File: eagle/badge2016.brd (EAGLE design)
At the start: 135 x 100.5 mm, 123 parts, among them IC1 25AA080SN, IC2 FT231XQ, J1 USB-MICRO, Q2 BC857ALT1SMD, Q2_24MHZ NX5032G, X1 PASSER-07, X10 PAD-1.27X1.27, X12 PAD-1.27X1.27, X13 PAD-1.27X1.27, X14 PAD-1.27X1.27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

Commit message: Final Badge!
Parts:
- added R13, R14: 100k, we-rcl:C0402
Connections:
- new net N$33: IC1.7, R14.2
- new net N$38: IC1.3, R13.2
- net 3V3: now also R13.1, R14.1
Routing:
- net N$38: track 0.00 -> 5.61 mm
- net EEPROM_!CS: track 27.8 -> 22.5 mm
- net N$33: track 0.00 -> 3.96 mm
- net 3V3: track 325.7 -> 329.2 mm
- net SPI_MOSI: track 82.3 -> 85.4 mm
- net SPI_MISO: track 63.0 -> 61.9 mm
- net GND: vias 354 -> 353
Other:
- board text added: "Silkscreen: T_PRINT 100 and B_PRINT 101"

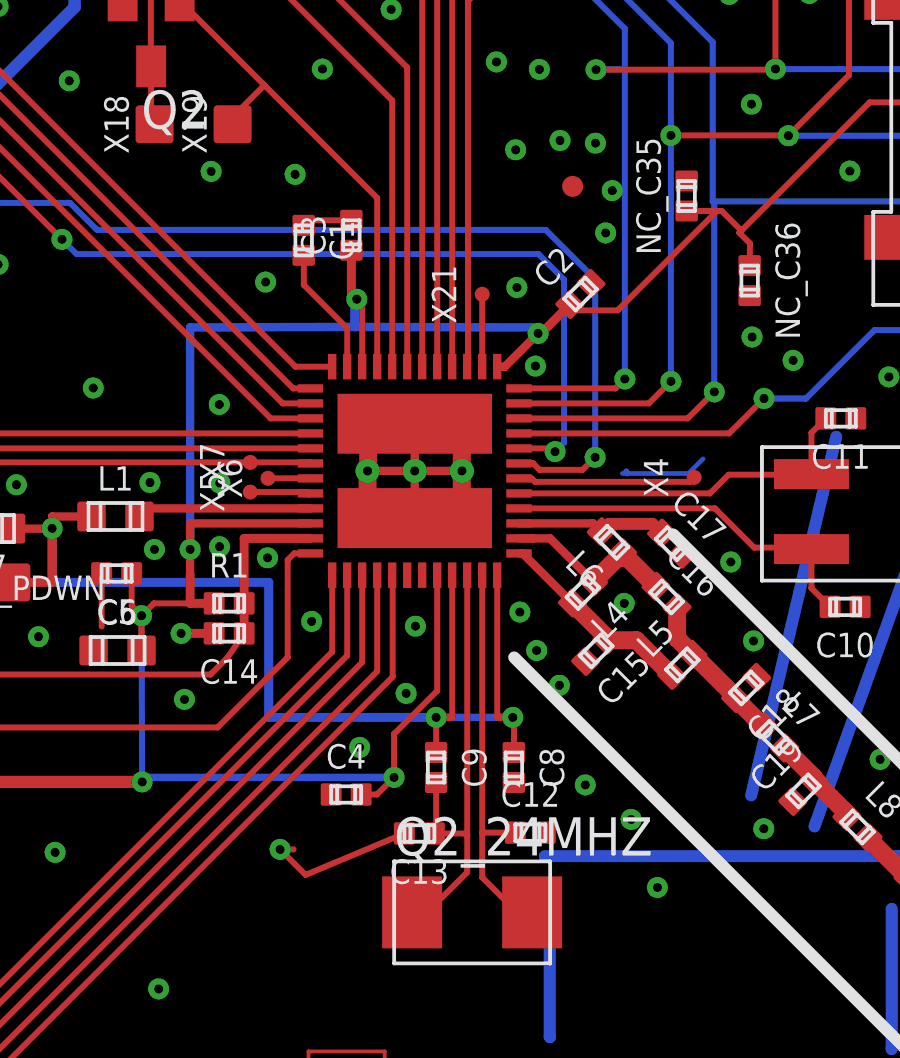
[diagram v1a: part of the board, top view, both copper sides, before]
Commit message: final badge with fixes from watterott
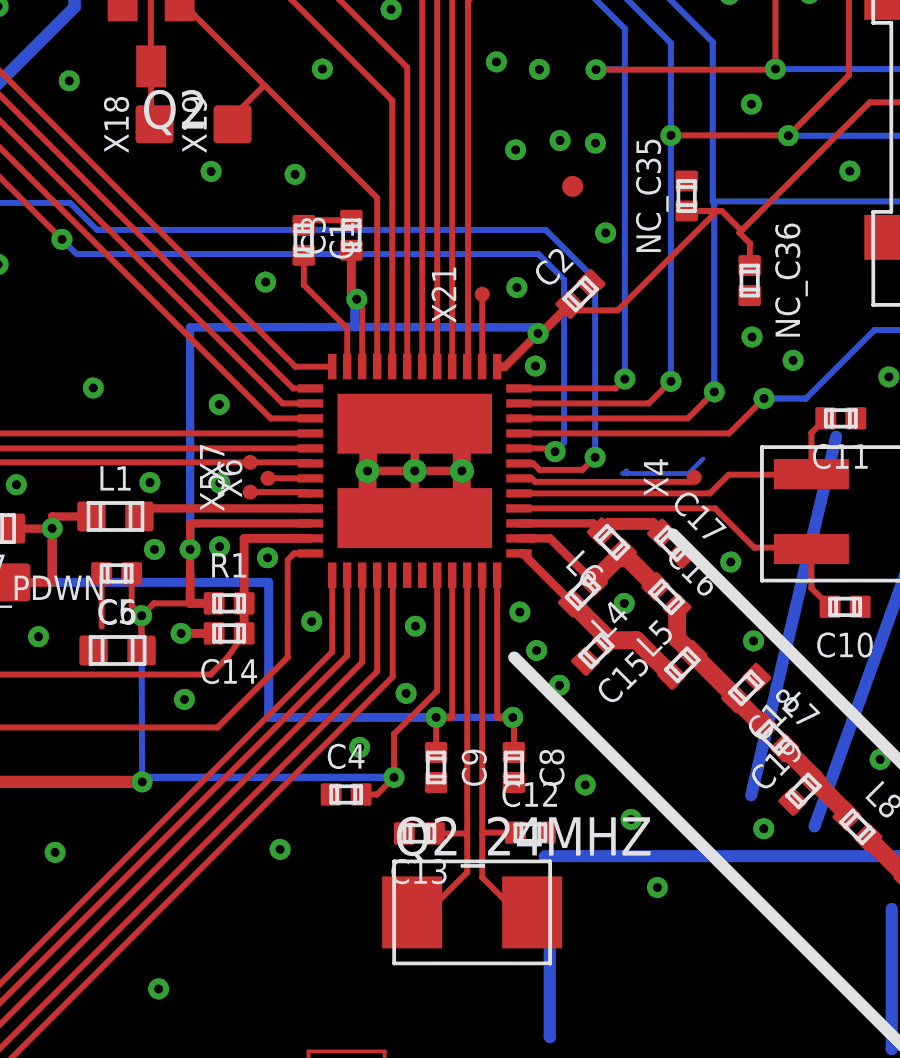
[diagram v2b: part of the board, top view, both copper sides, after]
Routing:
- net GND: track 200.7 -> 193.8 mm, vias 353 -> 352
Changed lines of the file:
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@@
 <via x="86.33" y="74.13" extent="1-16" drill="0.3"/>
 <via x="87.51" y="74.04" extent="1-16" drill="0.3"/>
-<via x="88.07" y="72.46" extent="1-16" drill="0.3"/>
 <via x="87.85" y="71.05" extent="1-16" drill="0.3"/>
 <via x="57.3" y="72" extent="1-16" drill="0.3"/>
@@
 <via x="77.84" y="95.305" extent="1-16" drill="0.3"/>
 <via x="79.71" y="95.295" extent="1-16" drill="0.3"/>
-<wire x1="82.2" y1="51" x2="82.2" y2="52.73" width="0.2" layer="1"/>
 <via x="77" y="50.5" extent="1-16" drill="0.3"/>
 <via x="89.575" y="49.23" extent="1-16" drill="0.3"/>
-<wire x1="81.14" y1="51.03" x2="77.85" y2="49.65" width="0.2" layer="1"/>
-<wire x1="77.85" y1="49.65" x2="77" y2="50.5" width="0.2" layer="1"/>
-<wire x1="77.45" y1="50.5" x2="77" y2="50.5" width="0.2" layer="1"/>
 <via x="73.1" y="1.2" extent="1-16" drill="0.3"/>
 <via x="81.6" y="0.7" extent="1-16" drill="0.3"/>

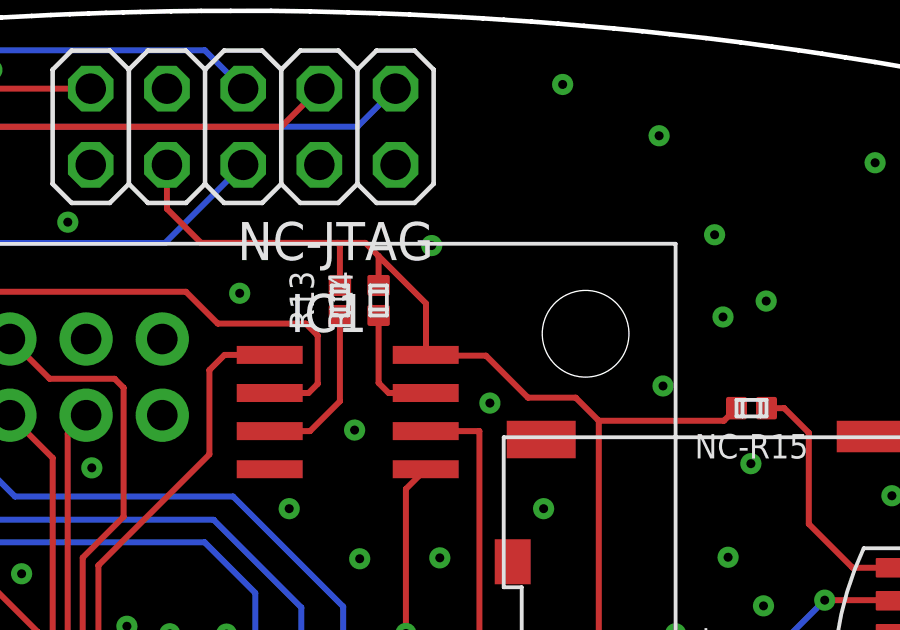
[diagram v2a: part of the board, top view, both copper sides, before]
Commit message: fixed final values in schematics: changed spi memory to 1M change loads of caps
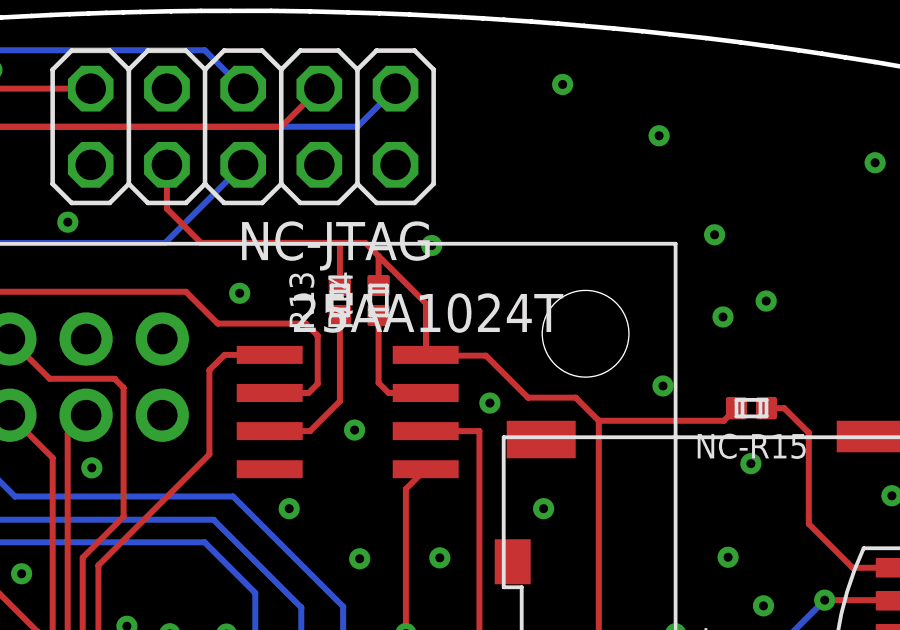
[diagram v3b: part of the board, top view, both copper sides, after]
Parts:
- 25AA1024T: value 25AA080SN -> 25AA1024T
- renumbered IC1 to 25AA1024T
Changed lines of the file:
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@@
 <element name="R20" library="we-rcl" package="C0402" value="1k5" x="18.265" y="70.39" rot="R90"/>
 <element name="U$15" library="ERNW_parts" package="JST-2" value="JST-2" x="47.2" y="39" rot="R180"/>
-<element name="IC1" library="microchip" package="SO-08" value="25AA080SN" x="91.57" y="83.89" rot="R270">
+<element name="25AA1024T" library="microchip" package="SO-08" value="25AA1024T" x="91.57" y="83.89" rot="R270">
 <attribute name="OC_NEWARK" value="92C7351" x="91.57" y="83.89" size="1.778" layer="27" rot="R270" display="off"/>
 <attribute name="MPN" value="25AA080/SN" x="91.57" y="83.89" size="1.778" layer="27" rot="R270" display="off"/>
@@
 <via x="72.22" y="94.03" extent="1-16" drill="0.3"/>
 <via x="71.44" y="92.82" extent="1-16" drill="0.3"/>
-<contactref element="IC1" pad="4"/>
+<contactref element="25AA1024T" pad="4"/>
 <via x="94.64" y="79.03" extent="1-16" drill="0.3"/>
 <via x="91.97" y="79" extent="1-16" drill="0.3"/>
@@
 <wire x1="92.65" y1="69.96" x2="92.66" y2="70.7" width="0.2" layer="1"/>
 <wire x1="92.66" y1="70.7" x2="92.305" y2="71.055" width="0.2" layer="1"/>
-<contactref element="IC1" pad="8"/>
+<contactref element="25AA1024T" pad="8"/>
 <contactref element="NC-R15" pad="1"/>
 <contactref element="NC-R18" pad="1"/>
@@
 <wire x1="93.51" y1="76.51" x2="102.48" y2="76.51" width="0.2" layer="16"/>
 <wire x1="102.48" y1="76.51" x2="102.48" y2="76.52" width="0.2" layer="16"/>
-<contactref element="IC1" pad="5"/>
-<contactref element="IC1" pad="2"/>
+<contactref element="25AA1024T" pad="5"/>
+<contactref element="25AA1024T" pad="2"/>
 <wire x1="94.17" y1="81.985" x2="93.51" y2="81.325" width="0.2" layer="1"/>
 <wire x1="93.51" y1="81.325" x2="93.51" y2="76.51" width="0.2" layer="1"/>
@@
 <wire x1="93.94" y1="74.29" x2="102.525" y2="74.29" width="0.2" layer="16"/>
 <wire x1="102.525" y1="74.29" x2="102.525" y2="74.3" width="0.2" layer="16"/>
-<contactref element="IC1" pad="6"/>
+<contactref element="25AA1024T" pad="6"/>
 <wire x1="94.17" y1="83.255" x2="95.96" y2="83.255" width="0.2" layer="1"/>
 <wire x1="95.96" y1="83.255" x2="95.96" y2="76.31" width="0.2" layer="1"/>
@@
 </signal>
 <signal name="EEPROM_!CS">
-<contactref element="IC1" pad="1"/>
+<contactref element="25AA1024T" pad="1"/>
 <contactref element="U$1" pad="15"/>
 <wire x1="83.26" y1="78.78" x2="83.26" y2="66.615215625" width="0.2" layer="1"/>
@@
 </signal>
 <signal name="N$33">
-<contactref element="IC1" pad="7"/>
+<contactref element="25AA1024T" pad="7"/>
 <contactref element="R14" pad="2"/>
 <wire x1="92.6" y1="87.11" x2="92.6" y2="84.86" width="0.2" layer="1"/>
@@
 </signal>
 <signal name="N$38">
-<contactref element="IC1" pad="3"/>
+<contactref element="25AA1024T" pad="3"/>
 <contactref element="R13" pad="2"/>
 <wire x1="91.31" y1="87.11" x2="91.31" y2="84.25" width="0.2" layer="1"/>

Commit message: changed values of NC parts so that they'd appear in BOM added final BOM as sent to watterott
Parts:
- NC-R16, NC-R17, NC_R13: value 10k -> NC_10k
- NC_C35: value 100nF -> NC_100nF
- NC_C36: value 4.7µF -> NC_4.7µF
- NC_R14: value 0R -> NC_0R
- NC_R15, NC_R16, NC_R2, NC_R3: value 0 -> NC_0R
- NC_R18, NC_R19: value 0 -> NC_0
- NC_R5: value 1k5 -> NC_1k5
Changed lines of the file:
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@@
 <element name="C20" library="we-rcl" package="C0402" value="3.3pF" x="98.280665625" y="49.895390625" rot="R135"/>
 <element name="C21" library="we-rcl" package="C0402" value="100pF" x="99.8540625" y="47.60894375" rot="R225"/>
-<element name="NC_R2" library="we-rcl" package="C0603" value="0" x="102.16" y="47.26" rot="R270"/>
-<element name="NC_R3" library="we-rcl" package="C0603" value="0" x="100.2" y="45.23"/>
+<element name="NC_R2" library="we-rcl" package="C0603" value="NC_0R" x="102.16" y="47.26" rot="R270"/>
+<element name="NC_R3" library="we-rcl" package="C0603" value="NC_0R" x="100.2" y="45.23"/>
 <element name="L9" library="we-rcl" package="C0402" value="12nH" x="99.69" y="39.7" rot="R90"/>
 <element name="C22" library="we-rcl" package="C0402" value="1pF" x="100.2" y="42.18"/>
@@
 <element name="BTN_RESET" library="ERNW_parts" package="KSEM31G" value="KSEM31G" x="41.05" y="79.24" rot="R270"/>
 <element name="R12" library="we-rcl" package="C0402" value="0R" x="34.53" y="59.45" rot="R270"/>
-<element name="NC_R13" library="we-rcl" package="C0402" value="10k" x="31.66" y="59.45" rot="R270"/>
-<element name="NC_R14" library="we-rcl" package="C0402" value="0R" x="32.37" y="55.51" rot="R180"/>
+<element name="NC_R13" library="we-rcl" package="C0402" value="NC_10k" x="31.66" y="59.45" rot="R270"/>
+<element name="NC_R14" library="we-rcl" package="C0402" value="NC_0R" x="32.37" y="55.51" rot="R180"/>
 <element name="NC-IC3" library="microchip" package="SO-08" value="24AA01SN" x="59.4" y="65.995" rot="R270">
 <attribute name="OC_FARNELL" value="1331268" x="59.4" y="65.995" size="1.778" layer="27" rot="R270" display="off"/>
@@
 <attribute name="MF" value="MICROCHIP" x="59.4" y="65.995" size="1.778" layer="27" rot="R270" display="off"/>
 </element>
-<element name="NC-R16" library="we-rcl" package="C0402" value="10k" x="64.085" y="63.595" rot="R180"/>
-<element name="NC-R17" library="we-rcl" package="C0402" value="10k" x="64.09" y="66.035"/>
+<element name="NC-R16" library="we-rcl" package="C0402" value="NC_10k" x="64.085" y="63.595" rot="R180"/>
+<element name="NC-R17" library="we-rcl" package="C0402" value="NC_10k" x="64.09" y="66.035"/>
 <element name="NC-JP4" library="pinhead" package="2X08" value="" x="11.97" y="47" rot="R270"/>
 <element name="U$14" library="ERNW_parts" package="MI0283QT" value="MI0283QT" x="76.5" y="47" rot="R180"/>
@@
 <attribute name="DIGIKEY" value="WM9750TR-ND" x="110.77" y="74.85" size="1.778" layer="27" rot="R90" display="off"/>
 </element>
-<element name="NC_C35" library="we-rcl" package="C0402" value="100nF" x="90.55" y="72.28"/>
-<element name="NC_C36" library="we-rcl" package="C0402" value="4.7µF" x="92.65" y="69.46" rot="R180"/>
+<element name="NC_C35" library="we-rcl" package="C0402" value="NC_100nF" x="90.55" y="72.28"/>
+<element name="NC_C36" library="we-rcl" package="C0402" value="NC_4.7µF" x="92.65" y="69.46" rot="R180"/>
 <element name="R19" library="we-rcl" package="C0402" value="4k32" x="18.25" y="71.4" rot="R270"/>
 <element name="R20" library="we-rcl" package="C0402" value="1k5" x="18.265" y="70.39" rot="R90"/>
@@
 <element name="U$6" library="ERNW_parts" package="TR_PIGPEN" value="TR_PIGPEN" x="79.215" y="42.495" rot="R270"/>
 <element name="LOGO1" library="we-symbol" package="SPARK_TOP" value="LOGO-S_LAYER" x="38.57" y="12.895" rot="R270"/>
-<element name="NC_R15" library="we-rcl" package="C0603" value="0" x="29.94" y="30.75"/>
-<element name="NC_R16" library="we-rcl" package="C0603" value="0" x="35.025" y="30.735"/>
+<element name="NC_R15" library="we-rcl" package="C0603" value="NC_0R" x="29.94" y="30.75"/>
+<element name="NC_R16" library="we-rcl" package="C0603" value="NC_0R" x="35.025" y="30.735"/>
 <element name="X4" library="we-rcl" package="PAD-0.5" value="PAD-0.5" x="90.8" y="62.9"/>
 <element name="X5" library="we-rcl" package="PAD-0.5" value="PAD-0.5" x="76.005" y="62.41"/>
@@
 <element name="X17" library="we-rcl" package="PAD-1.27X1.27" value="PAD-1.27X1.27" x="16.265" y="69.065"/>
 <element name="NC_LED2" library="we-opto" package="C0603" value="" x="14.44" y="64.2" rot="R180"/>
-<element name="NC_R5" library="we-rcl" package="C0402" value="1k5" x="14.59" y="67.12"/>
+<element name="NC_R5" library="we-rcl" package="C0402" value="NC_1k5" x="14.59" y="67.12"/>
 <element name="X18" library="we-rcl" package="PAD-1.27X1.27" value="PAD-1.27X1.27" x="72.815" y="74.67"/>
 <element name="X19" library="we-rcl" package="PAD-1.27X1.27" value="PAD-1.27X1.27" x="75.415" y="74.67"/>
@@
 <element name="C35" library="we-rcl" package="C0603" value="2.2µF" x="48.81" y="54.255"/>
 <element name="X21" library="we-rcl" package="PAD-0.5" value="PAD-0.5" x="83.735" y="69.005"/>
-<element name="NC_R18" library="we-rcl" package="C0402" value="0" x="54.645" y="81.39" rot="R270"/>
-<element name="NC_R19" library="we-rcl" package="C0402" value="0" x="54.65" y="82.455" rot="R270"/>
+<element name="NC_R18" library="we-rcl" package="C0402" value="NC_0" x="54.645" y="81.39" rot="R270"/>
+<element name="NC_R19" library="we-rcl" package="C0402" value="NC_0" x="54.65" y="82.455" rot="R270"/>
 <element name="C36" library="we-rcl" package="C1206" value="100µF" x="46.25" y="53.9" rot="R180"/>
 <element name="R15" library="we-rcl" package="C0402" value="0R3" x="46.25" y="57.6" rot="R180"/>
